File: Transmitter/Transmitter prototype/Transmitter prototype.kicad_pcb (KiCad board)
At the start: 2 copper layers, 23.5 x 33.6 mm, 15 parts, among them J1 Conn_Coaxial, J2 Conn_01x02, J3 Conn_01x03, J4 Conn_01x02_Socket, U1 OPA3692IDBQT

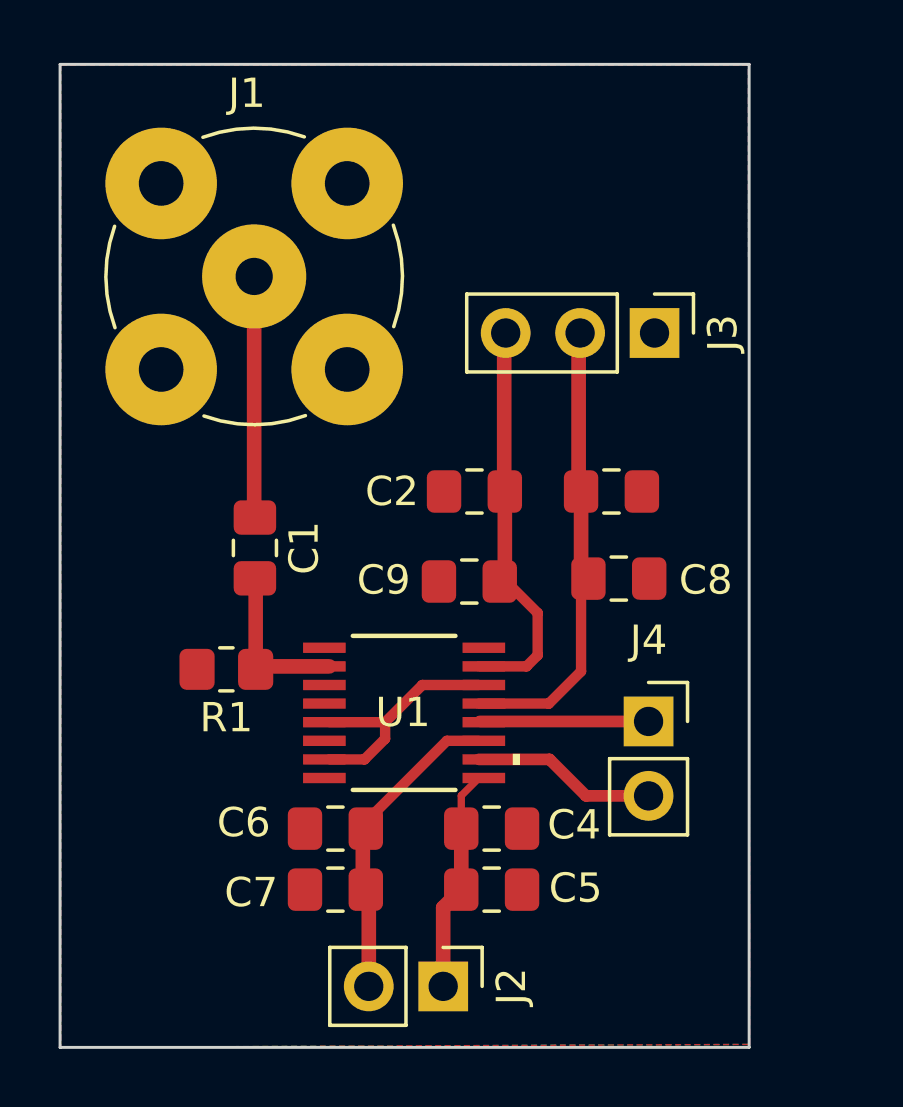
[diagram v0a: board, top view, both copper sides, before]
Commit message: Changed coax footprint for TX added pinheaders for test points for out A and coil start / end
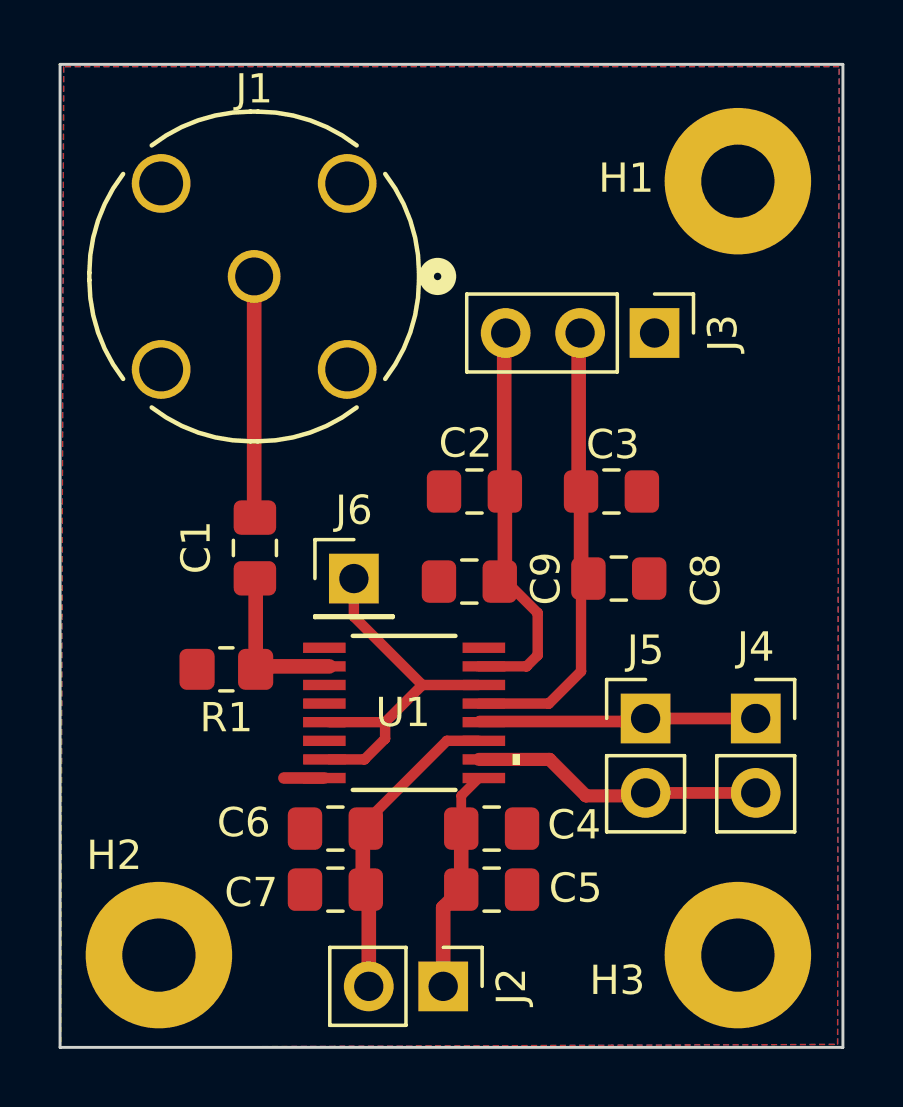
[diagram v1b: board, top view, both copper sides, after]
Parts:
- added H1: MountingHole, MountingHole:MountingHole_2.5mm_Pad, F.Cu at (179.7, 73.6)
- added H2: MountingHole, MountingHole:MountingHole_2.5mm_Pad, F.Cu at (159.9, 100.0)
- added H3: MountingHole, MountingHole:MountingHole_2.5mm_Pad, F.Cu at (179.7, 100.0)
- added J5: Conn_01x02, Connector_PinHeader_2.54mm:PinHeader_1x02_P2.54mm_Vertical, F.Cu at (176.5, 91.9)
- added J6: Conn_01x01, Connector_PinHeader_2.54mm:PinHeader_1x01_P2.54mm_Vertical, F.Cu at (166.6, 87.2)
- J1: footprint Connector_Coaxial:BNC_TEConnectivity_1478204_Vertical -> Amphenol 112404:CONN_112404_AMP
- moved J4 3.66 mm to (180.3, 91.9)
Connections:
- net Net-(J4-Pin_1) renamed /coil start
- net Net-(J4-Pin_2) renamed /coil end
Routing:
- net Net-(J6-Pin_1): track 8.39 -> 13.0 mm
- net /coil start: track 5.77 -> 9.52 mm
- net /coil end: track 6.31 -> 10.1 mm
- net GND: track 0.00 -> 1.38 mm
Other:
- board size 23.5 x 33.6 mm -> 26.7 x 33.6 mm

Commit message: added footprints for SOIC and SSOP for OPA3692
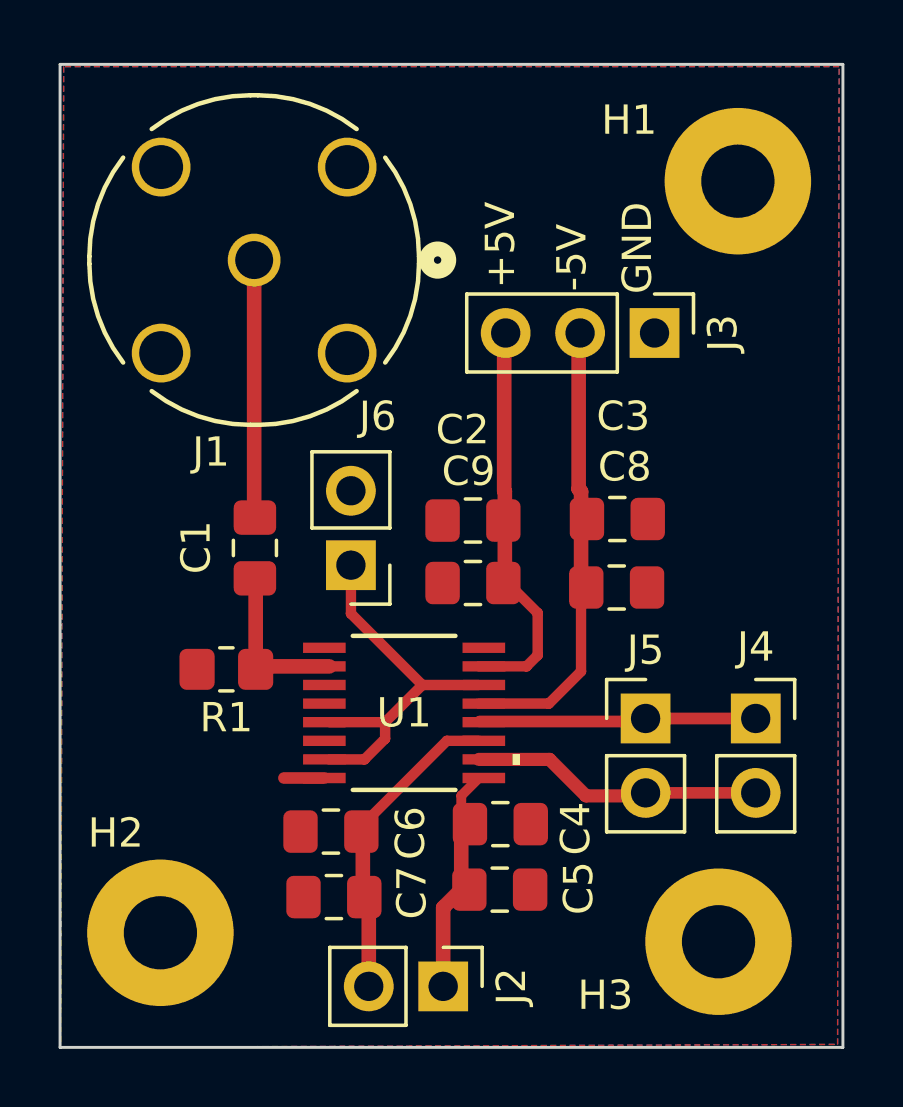
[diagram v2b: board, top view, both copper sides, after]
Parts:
- J6: value Conn_01x01 -> Conn_01x02; footprint Connector_PinHeader_2.54mm:PinHeader_1x01_P2.54mm_Vertical -> Connector_PinHeader_2.54mm:PinHeader_1x02_P2.54mm_Vertical
- moved C2 0.99 mm to (170.6, 85.2)
- moved C3 0.96 mm to (175.6, 85.1)
- moved H3 0.80 mm to (179.0, 99.6)
- moved H2 0.76 mm to (160.0, 99.3)
- moved J1 0.56 mm to (163.2, 76.3)
- moved J6 0.47 mm to (166.5, 86.7), turned to 180 degrees
- moved C4 0.33 mm to (171.6, 95.6)
- moved C8 0.31 mm to (175.5, 87.5)
- moved C5 0.28 mm to (171.6, 97.8)
- moved C7 0.26 mm to (165.9, 98.0)
- moved C6 0.18 mm to (165.8, 95.8)
- moved C9 0.13 mm to (170.6, 87.3)
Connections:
- J1 pad 3: (no net) -> GND
- J1 pad 4: (no net) -> GND
- J1 pad 5: (no net) -> GND
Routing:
- net Net-(J1-In): track 8.24 -> 8.83 mm
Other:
- board text added: "+5V"
- board text added: "-5V"
- board text added: "GND"
